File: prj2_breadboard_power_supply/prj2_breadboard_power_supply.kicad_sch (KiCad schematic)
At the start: 16 parts, among them J1 Conn_01x02_Pin, J2 Conn_01x02_Pin, J3 Conn_01x03_Pin, J4 Conn_01x03_Pin, J5 Screw_Terminal_01x02, J6 Barrel_Jack, U1 LM7805_TO220, U2 LM317_TO-220

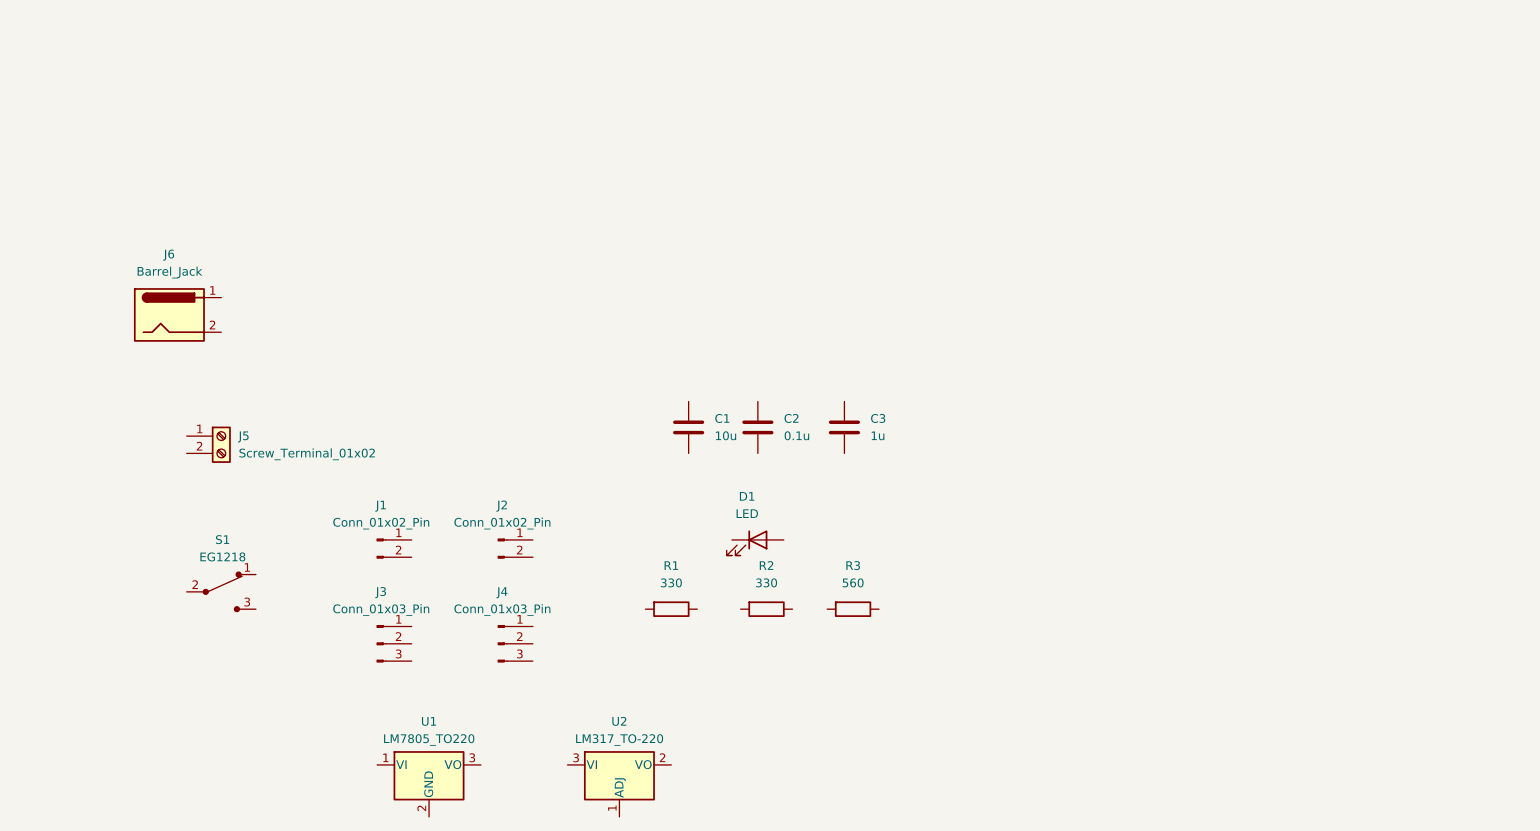
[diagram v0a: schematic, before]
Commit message: Schematico progetto 2
Feat: creato lo schema elettrico completo
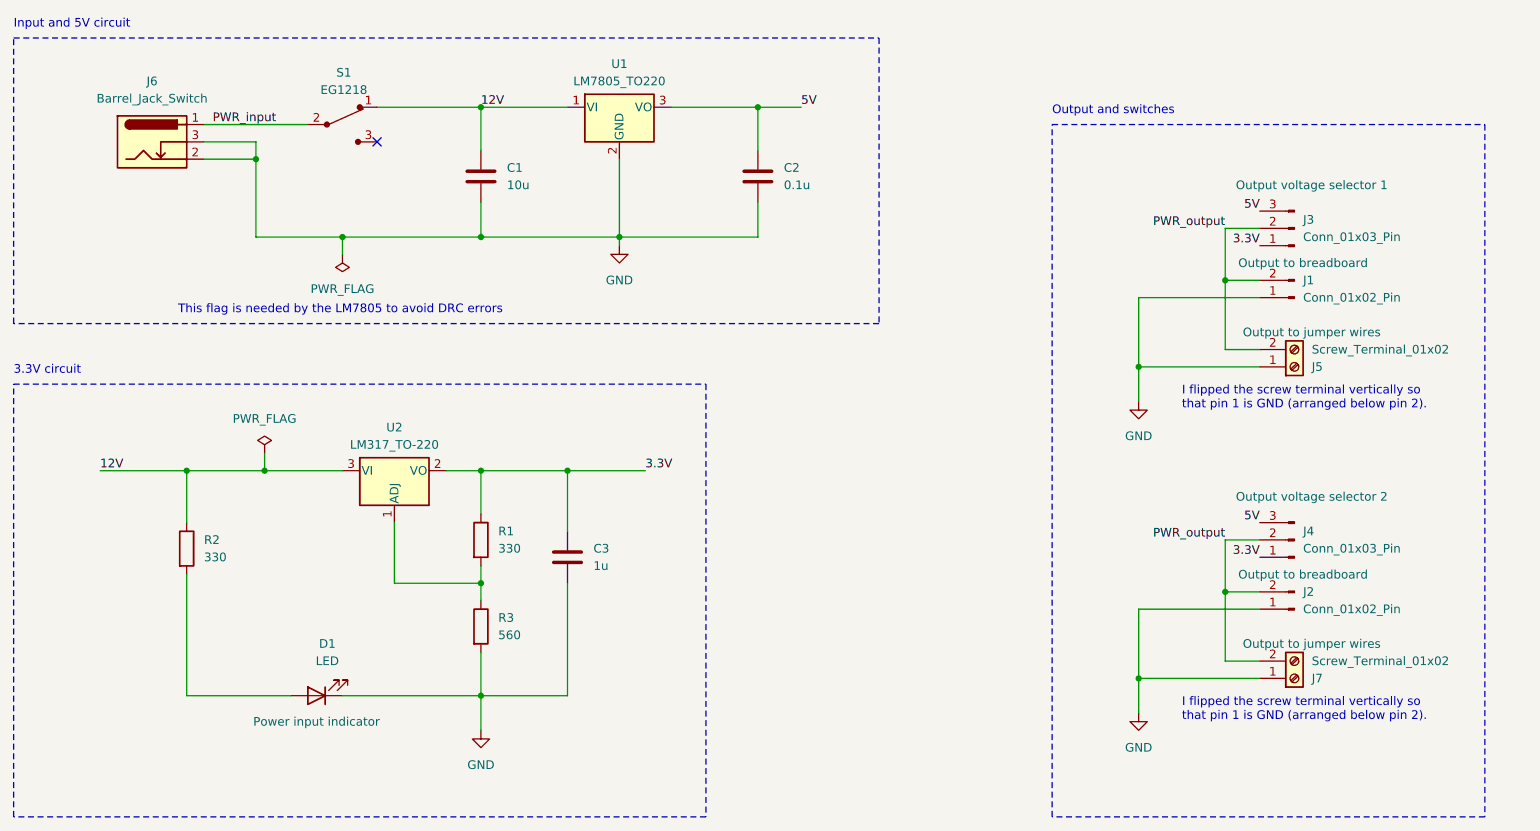
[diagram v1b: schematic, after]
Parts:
- removed J6: Barrel_Jack, symbol Connector:Barrel_Jack
- added J6: Barrel_Jack_Switch, Connector_BarrelJack:BarrelJack_Horizontal, symbol Connector:Barrel_Jack_Switch
- added J7: Screw_Terminal_01x02, TerminalBlock:TerminalBlock_bornier-2_P5.08mm, symbol Connector:Screw_Terminal_01x02
- C1, C2, C3: footprint (none) -> Capacitor_THT:C_Disc_D3.0mm_W1.6mm_P2.50mm
- D1: footprint (none) -> LED_THT:LED_D5.0mm; Purpose (none) -> Power input indicator
- J1, J2: footprint (none) -> Connector_PinHeader_2.54mm:PinHeader_1x02_P2.54mm_Vertical; Purpose (none) -> Output to breadboard
- J3: footprint (none) -> Connector_PinHeader_2.54mm:PinHeader_1x03_P2.54mm_Vertical; Purpose (none) -> Output voltage selector 1
- J4: footprint (none) -> Connector_PinHeader_2.54mm:PinHeader_1x03_P2.54mm_Vertical; Purpose (none) -> Output voltage selector 2
- J5: footprint (none) -> TerminalBlock:TerminalBlock_bornier-2_P5.08mm; Purpose (none) -> Output to jumper wires
- R1, R2, R3: footprint (none) -> Resistor_THT:R_Axial_DIN0204_L3.6mm_D1.6mm_P7.62mm_Horizontal
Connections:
- net GND: now reaches J2.1 (Pin_1)
- net GND: now also C1.2, C2.2, C3.2, D1.1 (K), J1.1 (Pin_1), J5.1 (Pin_1), R3.2, U1.2 (GND), J6.2, J6.3, J7.1 (Pin_1)
- net PWR_output: now reaches J2.2 (Pin_2)
- net PWR_output: now also J1.2 (Pin_2), J3.2 (Pin_2), J4.2 (Pin_2), J5.2 (Pin_2), J7.2 (Pin_2)
- net 3.3V: now reaches J4.1 (Pin_1)
- net 3.3V: now also C3.1, J3.1 (Pin_1), R1.1, U2.2 (VO)
- net 5V: now reaches J4.3 (Pin_3)
- net 5V: now also C2.1, J3.3 (Pin_3), U1.3 (VO)
- net 12V: now reaches S1.1
- net 12V: now also C1.1, R2.1, U1.1 (VI), U2.3 (VI)
- net PWR_input: now reaches S1.2
- net PWR_input: now also J6.1
- net at R3.1: now also R1.2, U2.1 (ADJ)
- net at D1.2 (A): now also R2.2
- no-connect marks 0 -> 1
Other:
- note added: "3.3V circuit"
- note added: "I flipped the screw terminal vertically so that pin 1 is GND (arranged below pin 2)."
- note added: "Input and 5V circuit"
- note added: "Output and switches"
- note added: "This flag is needed by the LM7805 to avoid DRC errors"
- moved on the sheet: C1, C2, C3, D1, J1, J2, J3, J4, J5, R1, R2, R3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

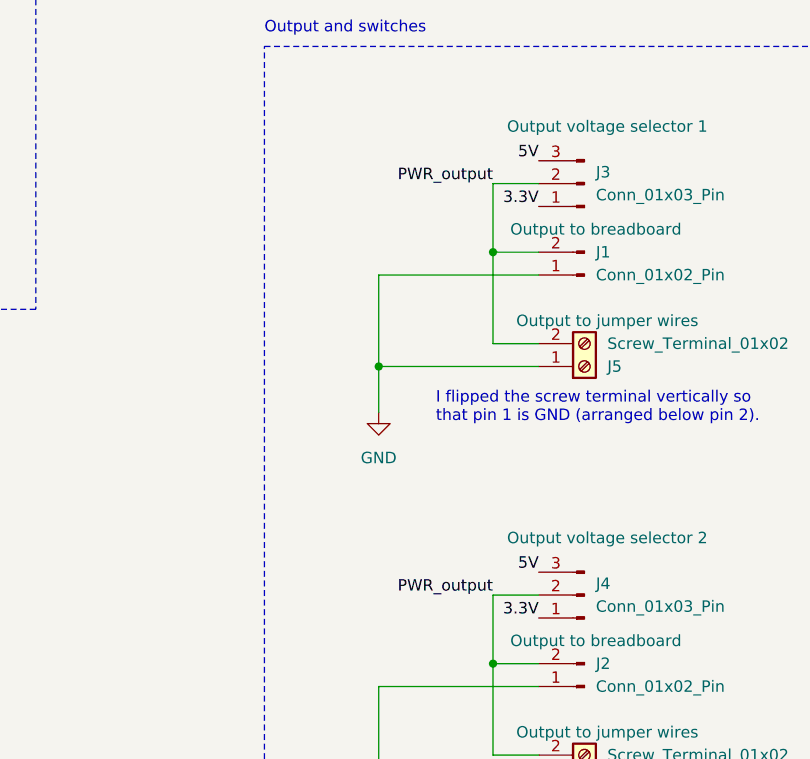
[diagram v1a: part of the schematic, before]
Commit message: Correzione schematico e PCB progetto 2
Fix: rimosso corto circuito tra pin 2 di J3 e J4
Feat: aggiornati i settaggi della pagina nel PCB
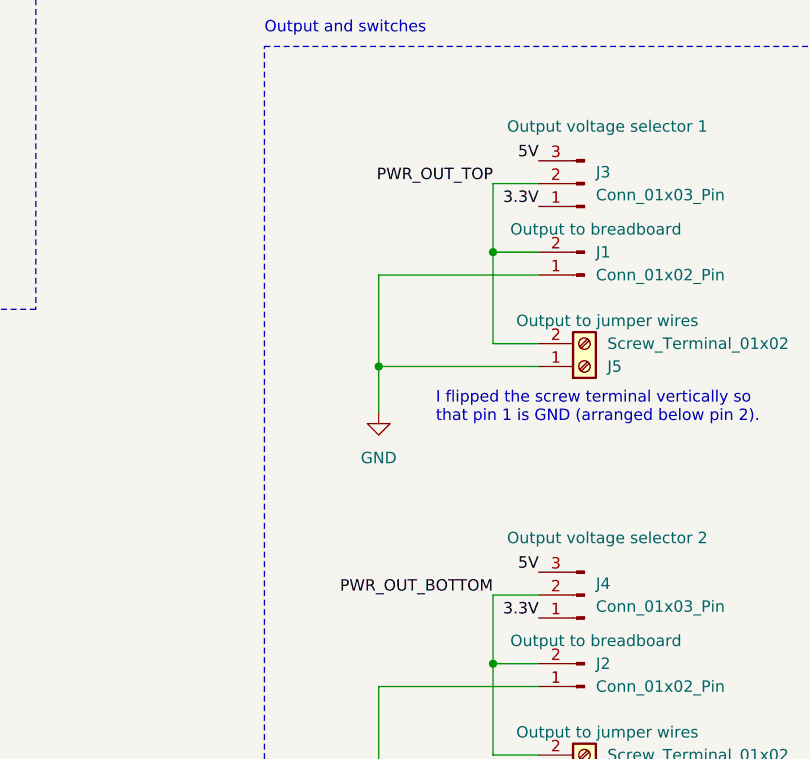
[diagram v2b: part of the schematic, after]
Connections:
- net PWR_output renamed PWR_OUT_BOTTOM
- net PWR_OUT_BOTTOM: no longer J1.2 (Pin_2), J3.2 (Pin_2), J5.2 (Pin_2)
- new net PWR_OUT_TOP: J1.2 (Pin_2), J3.2 (Pin_2), J5.2 (Pin_2)
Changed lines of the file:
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@@
     (effects (font (size 1.27 1.27)) (justify left bottom))
+  )
+  (label "PWR_OUT_TOP" (at 215.9 66.04 180) (fields_autoplaced)
+    (effects (font (size 1.27 1.27)) (justify right bottom))
+  )
+  (label "PWR_OUT_BOTTOM" (at 215.9 111.76 180) (fields_autoplaced)
+    (effects (font (size 1.27 1.27)) (justify right bottom))
   )
   (label "12V" (at 106.68 48.26 0) (fields_autoplaced)
     (effects (font (size 1.27 1.27)) (justify left bottom))
   )
-  (label "PWR_output" (at 215.9 66.04 180) (fields_autoplaced)
-    (effects (font (size 1.27 1.27)) (justify right bottom))
-  )
   (label "5V" (at 220.98 109.22 180) (fields_autoplaced)
     (effects (font (size 1.27 1.27)) (justify right bottom))
   )
-  (label "PWR_output" (at 215.9 111.76 180) (fields_autoplaced)
-    (effects (font (size 1.27 1.27)) (justify right bottom))
-  )
